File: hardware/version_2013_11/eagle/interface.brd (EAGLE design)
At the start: 63.9 x 21.7 mm, 19 parts

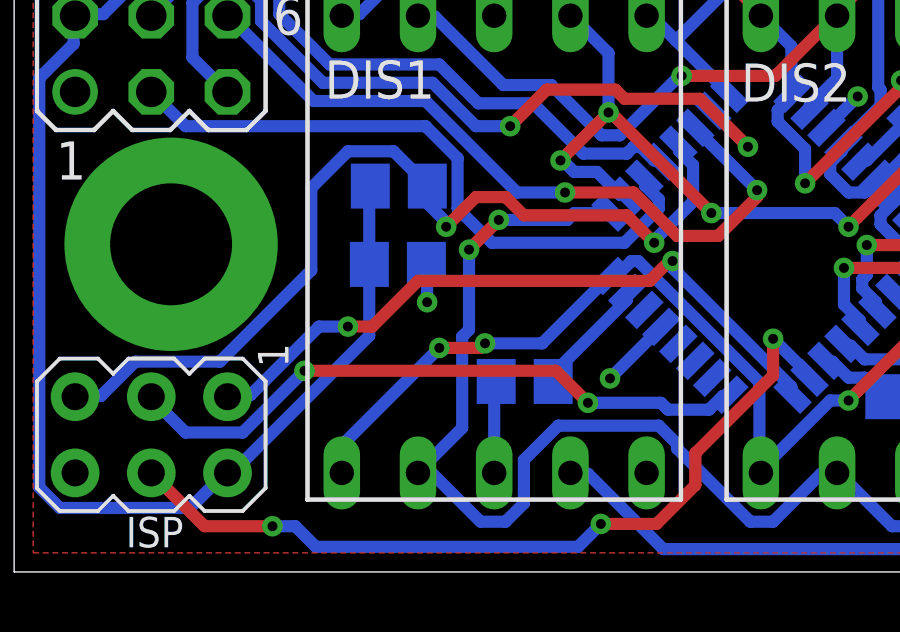
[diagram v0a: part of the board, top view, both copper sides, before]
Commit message: version 2013_11 was in fact newer, now corrected
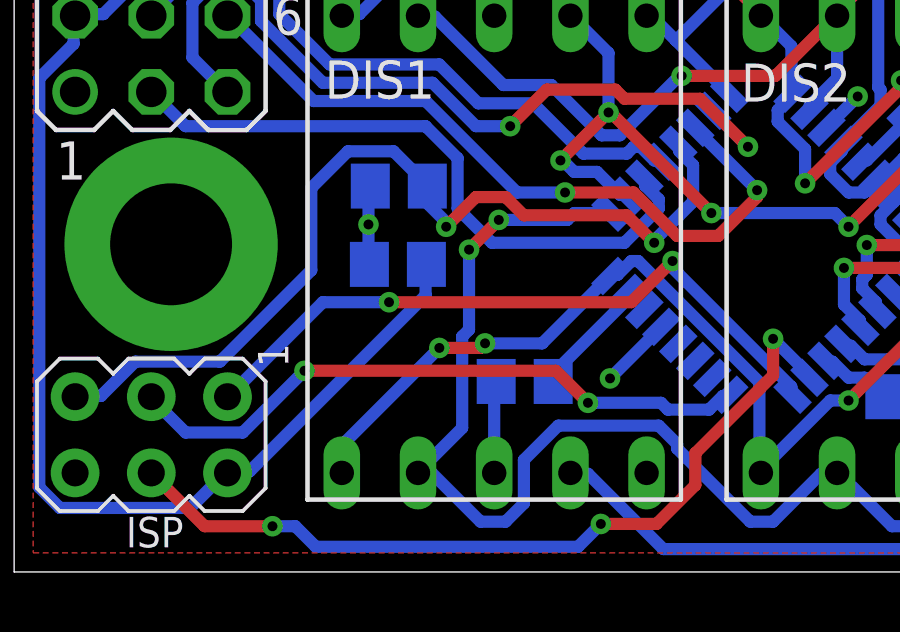
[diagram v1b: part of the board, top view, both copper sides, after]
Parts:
- turned C3 to 0 degrees
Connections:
- net +5V: no longer R1.1
- net GND: now also R1.1
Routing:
- net +5V: track 111.0 -> 109.5 mm
- net GND: track 14.6 -> 16.0 mm
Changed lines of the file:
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@@
 <autorouter>
 <pass name="Default">
-<param name="RoutingGrid" value="2mil"/>
+<param name="RoutingGrid" value="3mil"/>
 <param name="tpViaShape" value="round"/>
 <param name="PrefDir.1" value="*"/>
@@
 </autorouter>
 <elements>
-<element name="C3" library="rcl" package="C0805" value="100nF" x="12.792" y="10.252" smashed="yes" rot="MR180">
-<attribute name="NAME" x="10.379" y="12.482" size="1.27" layer="26" rot="MR180"/>
-<attribute name="VALUE" x="11.522" y="12.792" size="1.27" layer="28" rot="MR180"/>
+<element name="C3" library="rcl" package="C0805" value="100nF" x="12.792" y="10.252" smashed="yes" rot="MR0">
+<attribute name="NAME" x="15.205" y="8.022" size="1.27" layer="26" rot="MR0"/>
+<attribute name="VALUE" x="14.062" y="7.712" size="1.27" layer="28" rot="MR0"/>
 </element>
 <element name="R1" library="rcl" package="R0805" value="10k" x="12.822" y="12.862" smashed="yes" rot="MR180">
@@
 <attribute name="MF" value="" x="42.672" y="13.462" size="1.778" layer="28" rot="MR0" display="off"/>
 <attribute name="OC_FARNELL" value="unknown" x="42.672" y="13.462" size="1.778" layer="28" rot="MR0" display="off"/>
-<attribute name="NAME" x="45.077" y="11.176" size="0.762" layer="26" ratio="10" rot="MR0"/>
+<attribute name="NAME" x="46.347" y="11.176" size="1.27" layer="26" ratio="10" rot="MR0"/>
 <attribute name="VALUE" x="48.387" y="9.271" size="1.27" layer="28" ratio="10" rot="MR0"/>
 </element>
@@
 </element>
 <element name="C5" library="rcl" package="C0805" value="12-22pF" x="43.902" y="9.262" smashed="yes" rot="MR180">
-<attribute name="NAME" x="45.853" y="9.87" size="1.27" layer="26" rot="MR180"/>
+<attribute name="NAME" x="45.98" y="9.87" size="1.27" layer="26" rot="MR180"/>
 <attribute name="VALUE" x="42.632" y="11.802" size="1.27" layer="28" rot="MR180"/>
 </element>
@@
 </element>
 <element name="R2" library="rcl" package="R0805" value="220" x="17.018" y="6.35" smashed="yes" rot="MR180">
-<attribute name="NAME" x="12.827" y="6.731" size="1.27" layer="26" rot="MR180"/>
+<attribute name="NAME" x="13.081" y="6.731" size="1.27" layer="26" rot="MR180"/>
 <attribute name="VALUE" x="16.383" y="8.89" size="1.27" layer="28" rot="MR180"/>
 </element>
@@
 <signal name="GND">
 <contactref element="C3" pad="2"/>
+<contactref element="R1" pad="1"/>
 <contactref element="ATMEGA328P" pad="3"/>
 <contactref element="ATMEGA328P" pad="5"/>
@@
 <wire x1="28.2702" y1="13.716" x2="28.210171875" y2="13.67448125" width="0.4064" layer="16"/>
 <wire x1="30.0228" y1="15.1638" x2="30.06025" y2="15.19375" width="0.4064" layer="16"/>
+<wire x1="11.811" y1="12.8016" x2="11.811" y2="11.5824" width="0.4064" layer="16"/>
+<wire x1="11.811" y1="11.5824" x2="11.811" y2="10.287" width="0.4064" layer="16"/>
+<wire x1="11.811" y1="10.287" x2="11.842" y2="10.252" width="0.4064" layer="16"/>
+<wire x1="11.811" y1="12.8016" x2="11.872" y2="12.862" width="0.4064" layer="16"/>
 <wire x1="19.8628" y1="6.4516" x2="21.5646" y2="8.1534" width="0.4064" layer="16"/>
 <wire x1="21.5646" y1="8.1534" x2="21.57383125" y2="8.169515625" width="0.4064" layer="16"/>
@@
 <via x="19.8628" y="6.4516" extent="1-16" drill="0.3302"/>
 <via x="28.1178" y="15.8496" extent="1-16" drill="0.3302"/>
+<via x="11.811" y="11.5824" extent="1-16" drill="0.3302"/>
 <via x="31.0134" y="16.002" extent="1-16" drill="0.3302"/>
 <via x="40.0812" y="9.2964" extent="1-16" drill="0.3302"/>
-<wire x1="13.7668" y1="8.9916" x2="13.7668" y2="10.2108" width="0.4064" layer="16"/>
-<wire x1="13.7668" y1="10.2108" x2="13.742" y2="10.252" width="0.4064" layer="16"/>
-<via x="13.7668" y="8.9916" extent="1-16" drill="0.3302"/>
 </signal>
 <signal name="+5V">
@@
 <contactref element="LED1" pad="A"/>
 <contactref element="C1" pad="1"/>
+<wire x1="13.716" y1="9.2202" x2="13.716" y2="10.2108" width="0.4064" layer="16"/>
+<wire x1="7.8486" y1="3.3528" x2="13.716" y2="9.2202" width="0.4064" layer="16"/>
+<wire x1="7.1628" y1="3.3528" x2="7.8486" y2="3.3528" width="0.4064" layer="16"/>
+<wire x1="13.716" y1="10.2108" x2="13.742" y2="10.252" width="0.4064" layer="16"/>
+<wire x1="7.1628" y1="3.3528" x2="7.112" y2="3.302" width="0.4064" layer="16"/>
 <wire x1="1.9812" y1="17.6022" x2="1.9812" y2="18.5166" width="0.4064" layer="16"/>
 <wire x1="0.8382" y1="16.4592" x2="1.9812" y2="17.6022" width="0.4064" layer="16"/>
@@
 <wire x1="2.2098" y1="18.5928" x2="2.032" y2="18.542" width="0.4064" layer="16"/>
 <wire x1="27.7368" y1="14.4018" x2="27.644484375" y2="14.24016875" width="0.4064" layer="16"/>
-<contactref element="R1" pad="1"/>
-<wire x1="11.8364" y1="12.8524" x2="11.8364" y2="10.2616" width="0.4064" layer="16"/>
-<wire x1="11.8364" y1="10.2616" x2="11.842" y2="10.252" width="0.4064" layer="16"/>
-<wire x1="11.8364" y1="12.8524" x2="11.872" y2="12.862" width="0.4064" layer="16"/>
-<wire x1="11.8364" y1="7.874" x2="11.8364" y2="10.0584" width="0.4064" layer="16"/>
-<wire x1="7.3152" y1="3.3528" x2="11.8364" y2="7.874" width="0.4064" layer="16"/>
-<wire x1="11.8364" y1="10.0584" x2="11.842" y2="10.252" width="0.4064" layer="16"/>
-<wire x1="7.3152" y1="3.3528" x2="7.112" y2="3.302" width="0.4064" layer="16"/>
 </signal>
 <signal name="A">
@@
 <wire x1="21.9456" y1="10.1346" x2="25.908" y2="6.1722" width="0.4064" layer="16"/>
 <wire x1="21.9456" y1="10.3632" x2="21.9456" y2="10.1346" width="0.4064" layer="16"/>
+<wire x1="20.574" y1="8.9916" x2="21.9456" y2="10.3632" width="0.4064" layer="1"/>
+<wire x1="12.4968" y1="8.9916" x2="20.574" y2="8.9916" width="0.4064" layer="1"/>
+<wire x1="10.287" y1="8.9916" x2="12.4968" y2="8.9916" width="0.4064" layer="16"/>
+<wire x1="7.1628" y1="5.8674" x2="10.287" y2="8.9916" width="0.4064" layer="16"/>
 <wire x1="25.908" y1="5.9436" x2="25.947428125" y2="5.906771875" width="0.4064" layer="16"/>
 <wire x1="7.1628" y1="5.8674" x2="7.112" y2="5.842" width="0.4064" layer="16"/>
 <via x="21.9456" y="10.3632" extent="1-16" drill="0.3302"/>
-<wire x1="7.874" y1="5.8928" x2="7.366" y2="5.8928" width="0.4064" layer="16"/>
-<wire x1="10.16" y1="8.1788" x2="7.874" y2="5.8928" width="0.4064" layer="16"/>
-<wire x1="11.1252" y1="8.1788" x2="10.16" y2="8.1788" width="0.4064" layer="16"/>
-<wire x1="11.938" y1="8.1788" x2="11.1252" y2="8.1788" width="0.4064" layer="1"/>
-<wire x1="13.462" y1="9.7028" x2="11.938" y2="8.1788" width="0.4064" layer="1"/>
-<wire x1="21.1836" y1="9.7028" x2="13.462" y2="9.7028" width="0.4064" layer="1"/>
-<wire x1="21.844" y1="10.3632" x2="21.1836" y2="9.7028" width="0.4064" layer="1"/>
-<wire x1="21.9456" y1="10.3632" x2="21.844" y2="10.3632" width="0.4064" layer="1"/>
-<wire x1="7.366" y1="5.8928" x2="7.112" y2="5.842" width="0.4064" layer="16"/>
-<via x="11.1252" y="8.1788" extent="1-16" drill="0.3302"/>
+<via x="12.4968" y="8.9916" extent="1-16" drill="0.3302"/>
 </signal>
 <signal name="SCK">
